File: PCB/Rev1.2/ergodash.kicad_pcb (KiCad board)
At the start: 2 copper layers, 149.9 x 127.4 mm, 187 parts, among them J1 5PIN, J2 Conn_01x03, J3 Conn_01x03, J4 GS3, J5 GS3, M1 Speaker, Q1 IRLML6344TRPbF, SW1 SW_PUSH, SW10 SW_PUSH, SW11 SW_PUSH, SW12 SW_PUSH, SW13 SW_PUSH, SW14 SW_PUSH, SW15 SW_PUSH, SW16 SW_PUSH, SW17 SW_PUSH, SW18 SW_PUSH, SW19 SW_PUSH, SW2 SW_PUSH, SW20 SW_PUSH, SW21 SW_PUSH, SW22 SW_PUSH, SW23 SW_PUSH, SW24 SW_PUSH, SW25 SW_PUSH, SW26 SW_PUSH, SW27 SW_PUSH, SW28 SW_PUSH, SW29 SW_Push, SW3 SW_PUSH, SW30 SW_PUSH, SW31 SW_PUSH, SW32 SW_PUSH, SW33 SW_PUSH, SW34 SW_PUSH, SW35 SW_PUSH, SW36 SW_PUSH, SW37 SW_Push, SW38 SW_PUSH, SW39 SW_PUSH, SW4 SW_PUSH, SW40 SW_PUSH, SW41 SW_PUSH, SW5 SW_PUSH, SW6 SW_PUSH, SW7 SW_PUSH, SW8 SW_PUSH, SW9 SW_PUSH, U1 HOLE, U2 HOLE, U3 ProMicro, U4 HOLE, U5 HOLE, U6 ProMicro, U7 HOLE, U8 HOLE, U9 HOLE

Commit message: Rev 1.2 project cleanup
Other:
- net class Default removed

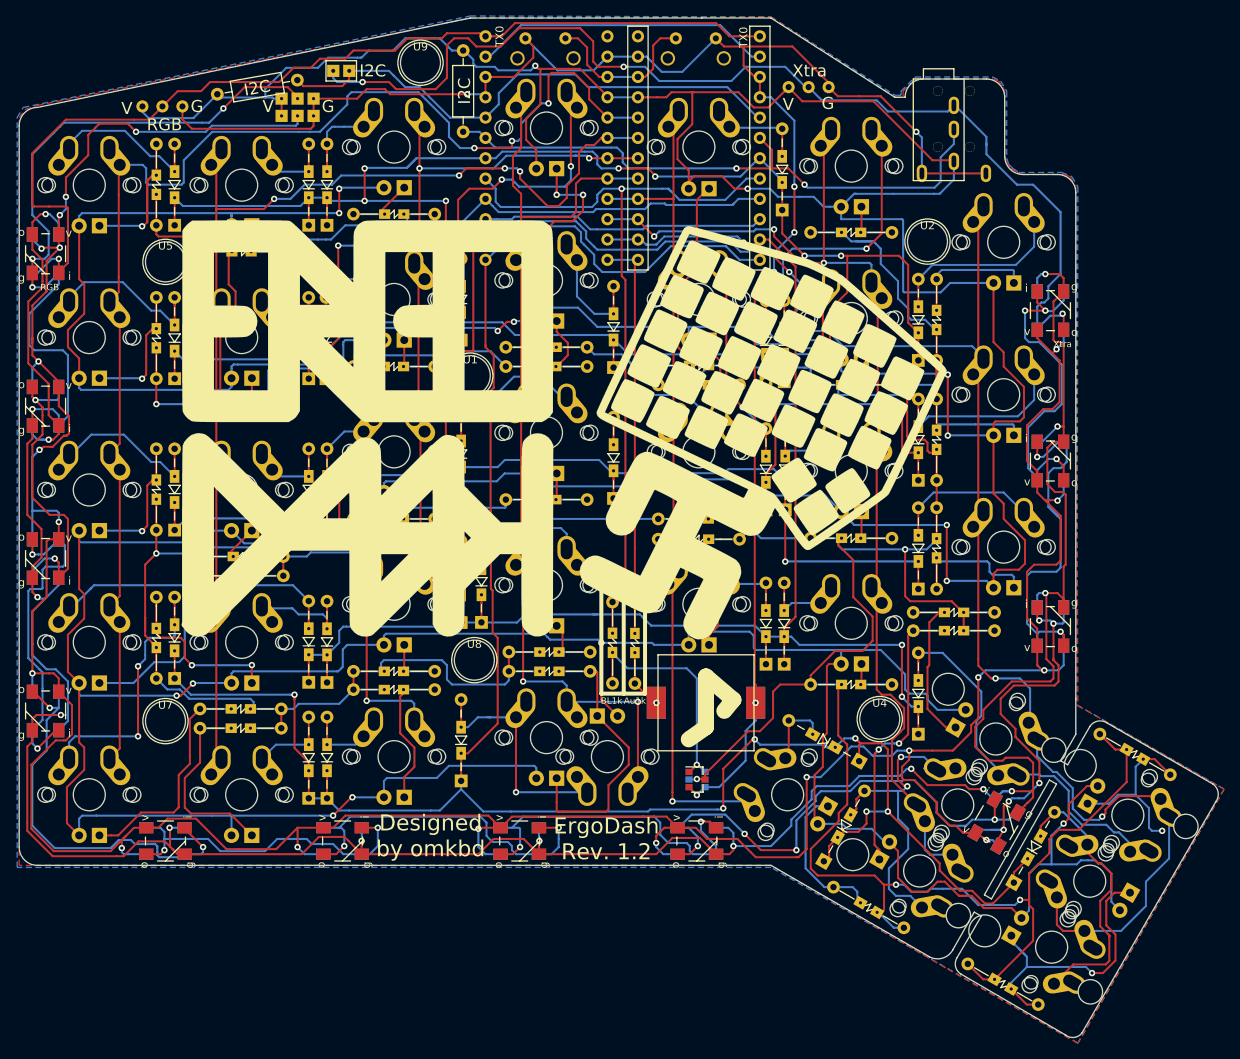
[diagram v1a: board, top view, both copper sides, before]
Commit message: Modified design for different logo
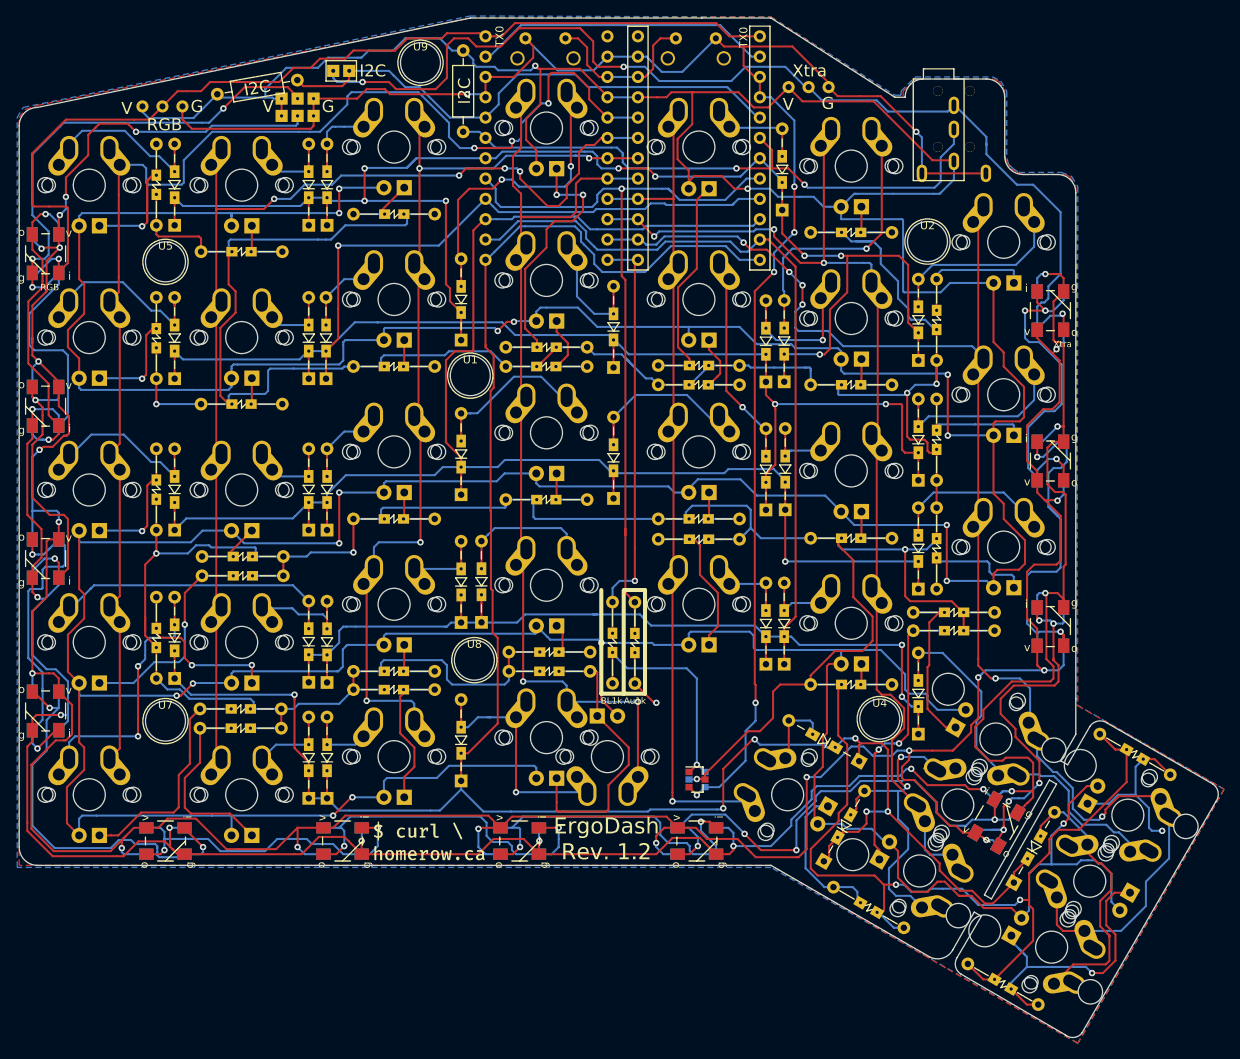
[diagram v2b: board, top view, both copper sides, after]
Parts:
- removed the G*** at (146.2, 88.5)
- removed the G*** at (146.6, 88.5)
- removed M1: Speaker, library:PKLCS1212E4001-R1
- added G***: LOGO, homerow-logos:homerow_2line, F.Cu at (129.6, 140.0)
- added G***: LOGO, homerow-logos:homerow_2line, B.Cu at (129.7, 140.0)
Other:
- board text removed: "Designed by omkbd"
